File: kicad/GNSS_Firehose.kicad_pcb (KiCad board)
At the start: 4 copper layers, 117.9 x 99.1 mm, 463 parts, among them J1 SMA, J10 HEADER_16, J2 SMA, J3 SMA, J4 SMA, J5 SMA, J6 HEADER_14, J7 L829-1J1T-43, J8 PJ-063BH, Q1 Si2369DS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

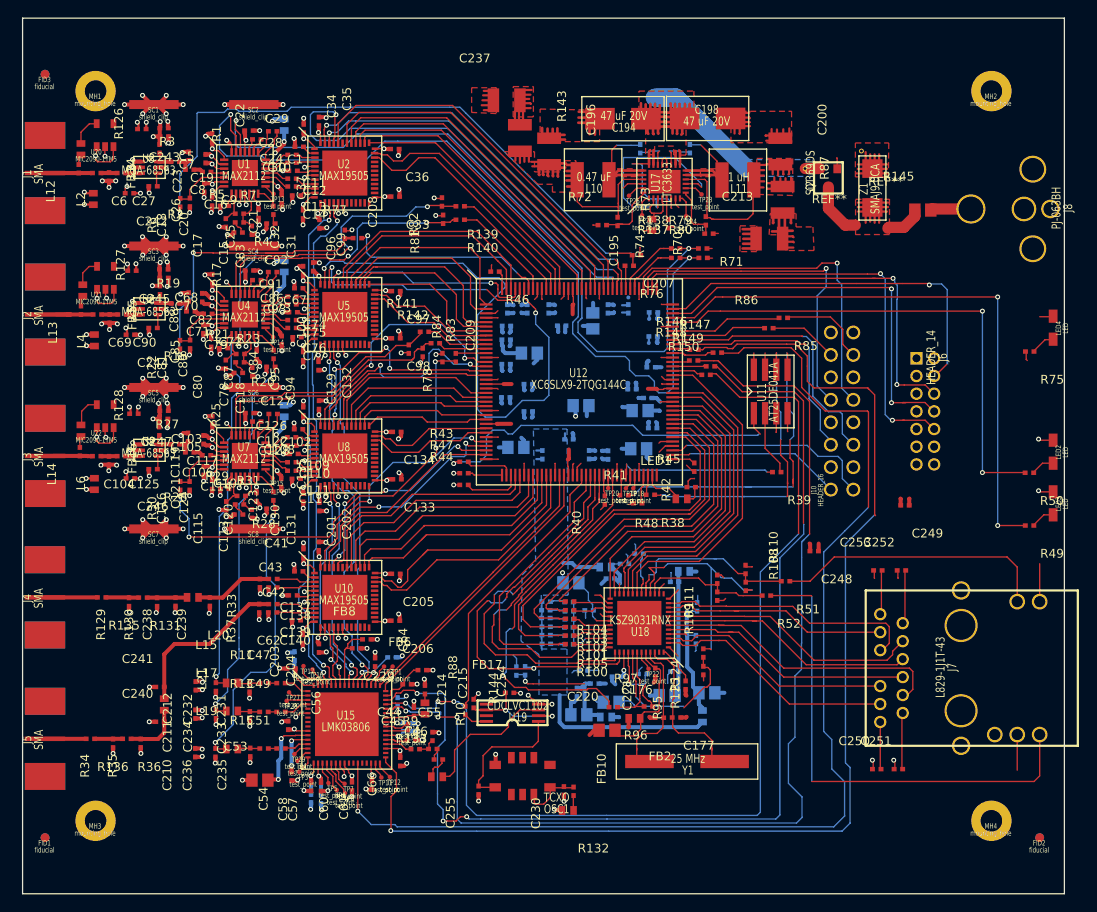
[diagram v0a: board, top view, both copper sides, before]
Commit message: add thermal vias to footprints
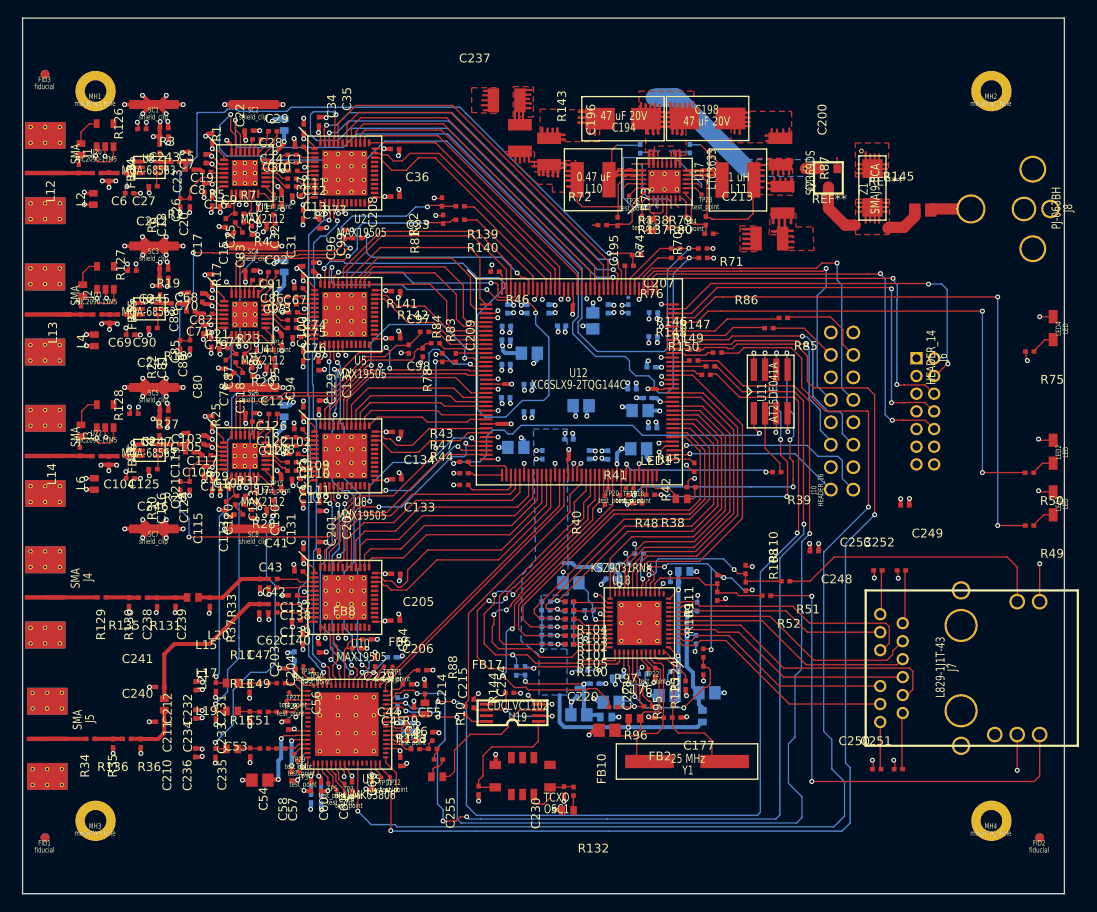
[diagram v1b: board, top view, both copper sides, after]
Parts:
- moved J5 0.24 mm to (73.4, 124.7)
- moved LED4 0.06 mm to (190.2, 78.3)
- turned C149 to 180 degrees
- turned C150 to 270 degrees
- turned C151 to 270 degrees
- turned C152 to 270 degrees
- turned C161 to 270 degrees
- turned C163 to 270 degrees
- turned C164 to 180 degrees
- turned C165 to 180 degrees
- turned C167 to 180 degrees
- turned C168 to 180 degrees
- turned C185 to 180 degrees
- turned C187 to 180 degrees
- turned C216 to 180 degrees
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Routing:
- net (no net): track 200.2 -> 51.1 mm
- net Net-(R48-Pad2): track 2.53 -> 36.8 mm, vias 0 -> 4
- net Net-(R38-Pad2): track 2.81 -> 33.9 mm, vias 0 -> 4
- net Net-(J7-Pad17): track 35.5 -> 56.5 mm, vias 0 -> 2
- net /Ethernet/DVDDH: track 42.8 -> 63.5 mm, vias 2 -> 10
- net /FPGA/din: track 1.98 -> 18.5 mm, vias 0 -> 2
- net /Ethernet/phyad0: track 9.13 -> 20.7 mm, vias 0 -> 2
- net /Ethernet/LED_MODE: track 12.8 -> 19.0 mm, vias 0 -> 2
- net GND: track 432.8 -> 430.1 mm, vias 227 -> 304
- net /Ethernet/AVDDH: track 17.5 -> 20.1 mm, vias 0 -> 2
- net PHY_MDIO: track 41.9 -> 44.2 mm, vias 0 -> 3
- net /Ethernet/DVDDL: track 22.9 -> 25.2 mm, vias 1 -> 7
- net CH2_GC1_FPGA_LPF: track 34.3 -> 32.1 mm
- net PHY_MDINT: track 44.4 -> 46.5 mm, vias 1 -> 3
- net VCC_3.3V: track 166.1 -> 164.5 mm, vias 55 -> 104
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
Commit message: all nets connected
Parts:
- added REF**: via_12mil, footprints:via_12mil, F.Cu at (134.2, 61.6)
- added REF**: via_12mil, footprints:via_12mil, F.Cu at (131.0, 53.9)
- added REF**: via_12mil, footprints:via_12mil, F.Cu at (125.2, 52.4)
- added REF**: via_12mil, footprints:via_12mil, F.Cu at (169.4, 67.0)
- added REF**: via_12mil, footprints:via_12mil, F.Cu at (162.0, 68.7)
- added REF**: via_12mil, footprints:via_12mil, F.Cu at (158.0, 61.2)
- added REF**: via_12mil, footprints:via_12mil, F.Cu at (155.4, 68.2)
- added REF**: via_12mil, footprints:via_12mil, F.Cu at (157.4, 55.1)
- added REF**: via_12mil, footprints:via_12mil, F.Cu at (145.7, 52.4)
- added REF**: via_12mil, footprints:via_12mil, F.Cu at (135.1, 54.7)
- moved J8 0.10 mm to (193.0, 64.8)
- turned C148 to 270 degrees
- turned C166 to 180 degrees
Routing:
- net (no net): track 51.1 -> 0.39 mm
- net Net-(C194-Pad1): track 31.0 -> 60.5 mm, vias 0 -> 3
- net VCC_1.2V: track 58.7 -> 88.1 mm, vias 12 -> 13
- net Net-(C195-Pad1): track 12.3 -> 30.8 mm, vias 0 -> 4
- net Net-(Q1-Pad3): track 20.2 -> 21.9 mm
- net Net-(C6-Pad1): track 6.84 -> 5.36 mm
- net Net-(C69-Pad1): track 4.65 -> 5.45 mm
- net GND: track 430.1 -> 429.9 mm, vias 304 -> 310
- net Net-(C199-Pad2): vias 0 -> 1
- net Net-(C197-Pad1): vias 0 -> 1
- net Net-(C199-Pad1): vias 0 -> 1
- net Net-(C197-Pad2): vias 0 -> 1

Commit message: layout passes DRC
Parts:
- added G***: LOGO, footprints:diff-bottom, F.Cu at (132.5, 92.7)
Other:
- net class Default: clearance 0.14986 -> 0.00508
- net class wide: clearance 0.14986 -> 0.00508
- rule trace_clearance: 0.14986 -> 0.00508
